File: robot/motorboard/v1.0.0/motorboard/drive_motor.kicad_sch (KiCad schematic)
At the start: 2 parts

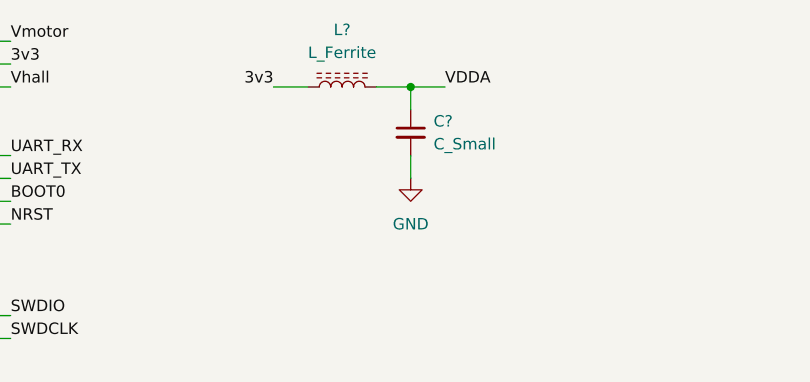
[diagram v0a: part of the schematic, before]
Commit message: finished MCU, SD, LED, DIP, and Vbatt mon. cube_hal updated
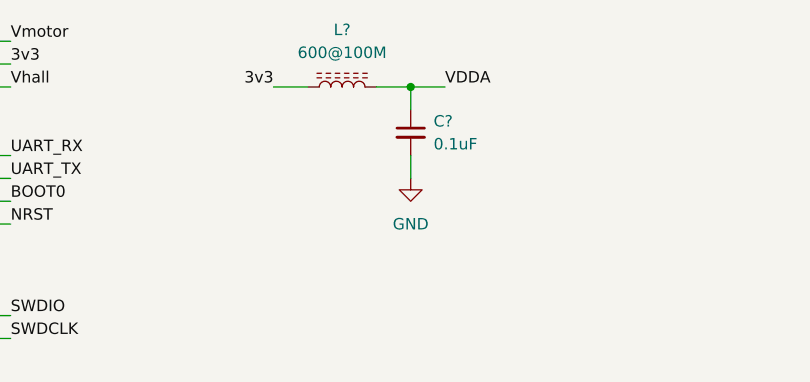
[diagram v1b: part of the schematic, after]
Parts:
- C?: value C_Small -> 0.1uF
- L?: value L_Ferrite -> 600@100M
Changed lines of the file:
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@@
     (in_bom yes) (on_board yes)
     (property "Reference" "L?" (id 0) (at 74.93 19.05 90))
-    (property "Value" "L_Ferrite" (id 1) (at 74.93 21.59 90))
+    (property "Value" "600@100M" (id 1) (at 74.93 21.59 90))
     (property "Footprint" "" (id 2) (at 74.93 25.4 0)
       (effects (font (size 1.27 1.27)) hide)
     )
-    (property "Datasheet" "~" (id 3) (at 74.93 25.4 0)
+    (property "Datasheet" "https://www.digikey.com/en/products/detail/tdk-corporation/MMZ1608B601CTAH0/600533" (id 3) (at 74.93 25.4 0)
       (effects (font (size 1.27 1.27)) hide)
     )
@@
       (effects (font (size 1.27 1.27)) (justify left))
     )
-    (property "Value" "C_Small" (id 1) (at 85.09 31.7499 0)
+    (property "Value" "0.1uF" (id 1) (at 85.09 31.7499 0)
       (effects (font (size 1.27 1.27)) (justify left))
     )

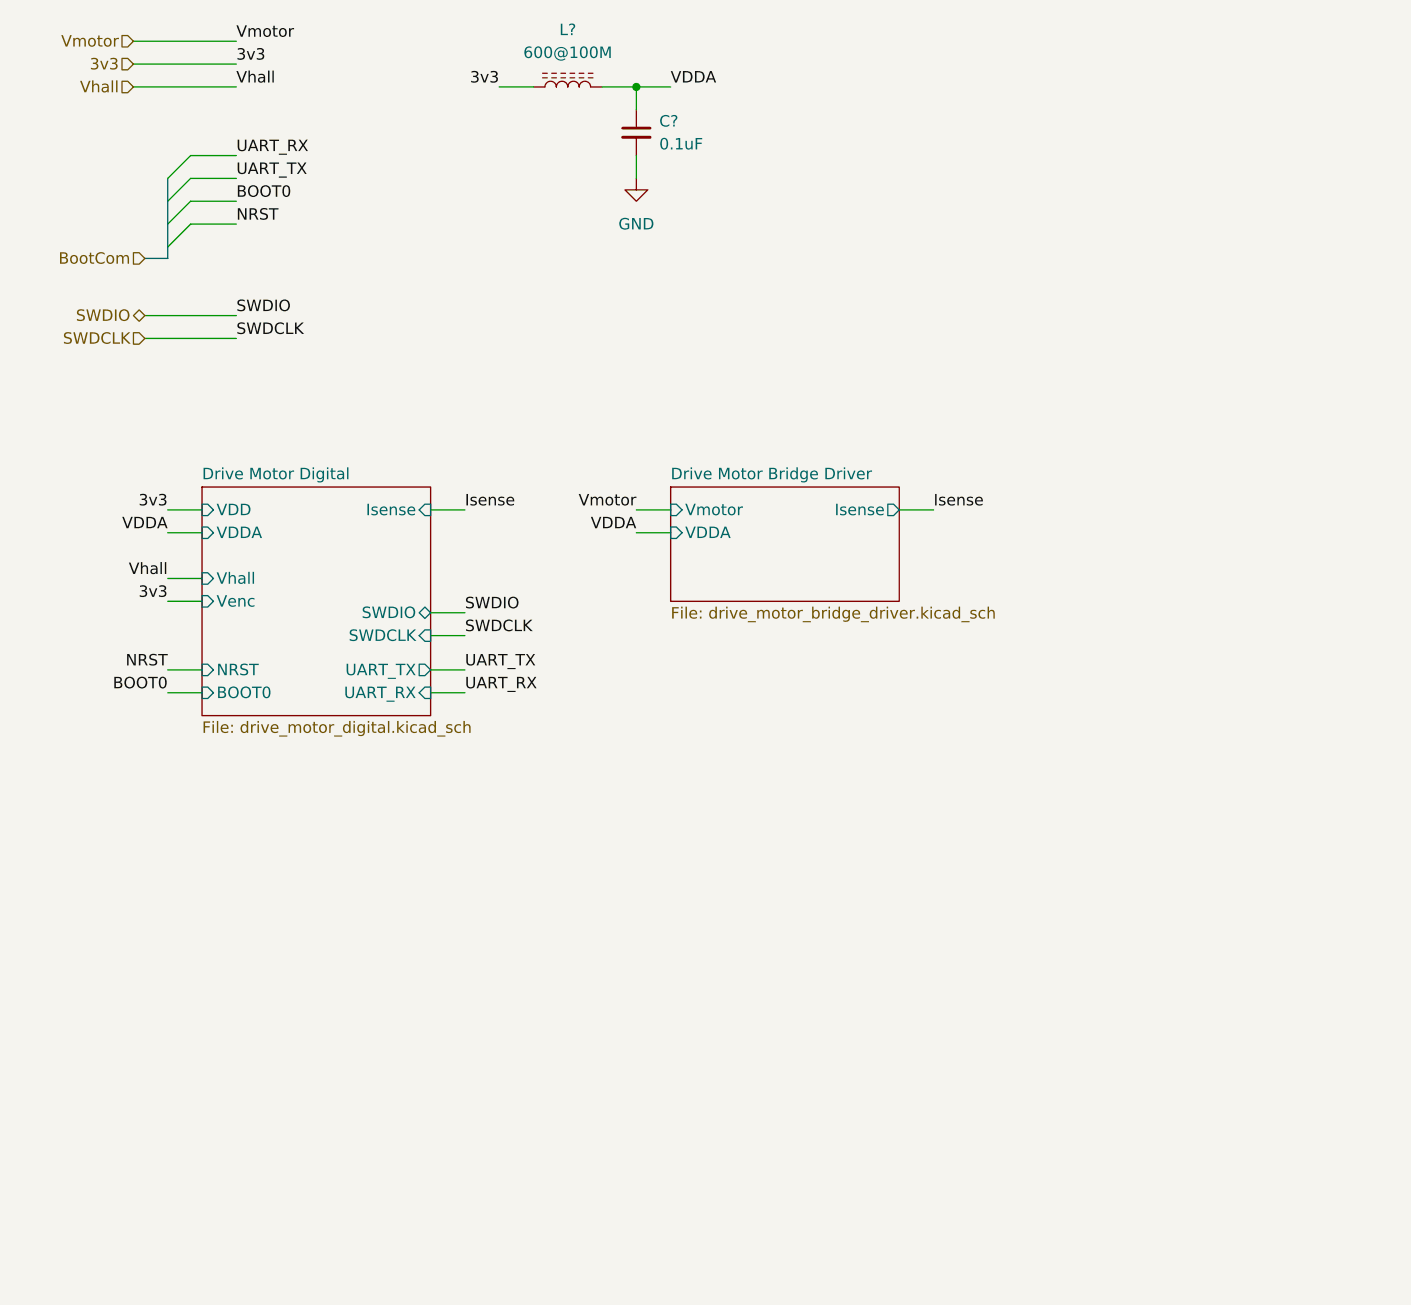
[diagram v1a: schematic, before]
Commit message: added top level bus aliases, other top level dev
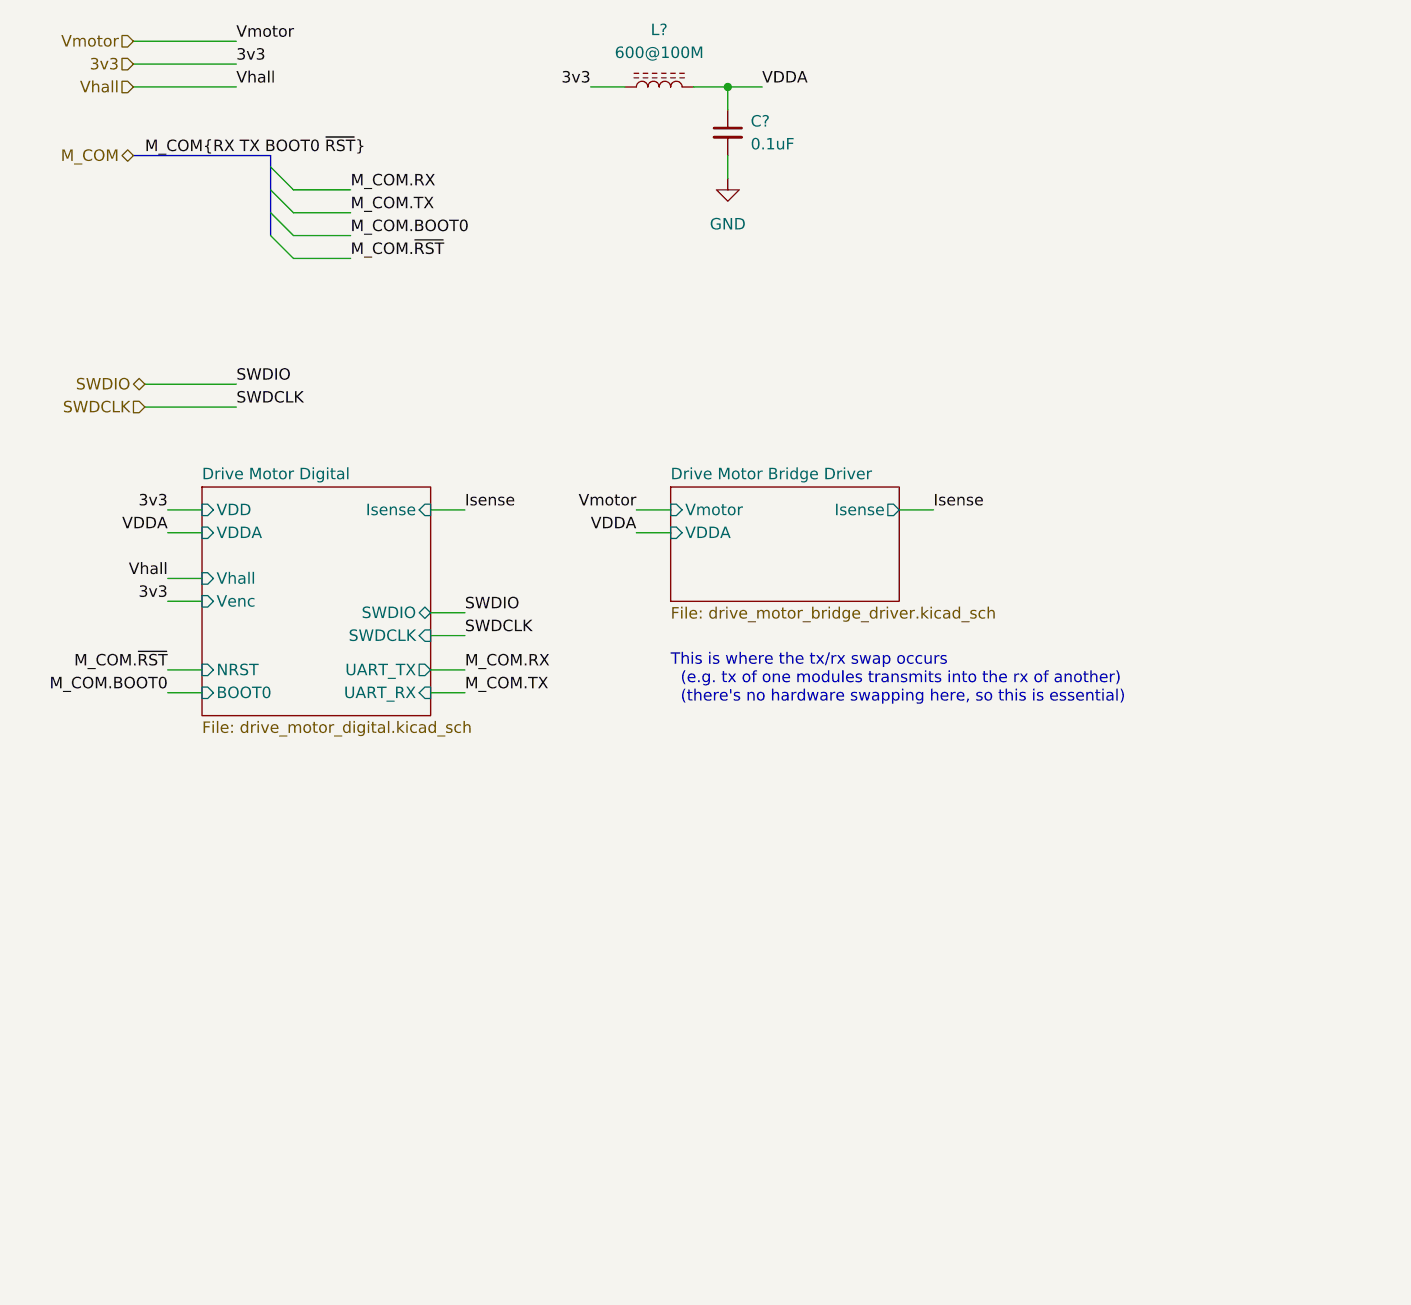
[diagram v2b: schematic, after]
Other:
- note added: "This is where the tx/rx swap occurs (e.g. tx of one modules transmits into the rx of another) (there's no hardware swapping here, so this is essential)"
- moved on the sheet: C?, L?

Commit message: bus name ERC fixes
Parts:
- gave numbers to parts that had none: 2
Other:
- sheet Drive Motor Bridge Driver ports: added {SENSE}; removed Isense
- sheet Drive Motor Digital ports: added {SENSE}; removed Isense
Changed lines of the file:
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@@
 (kicad_sch (version 20210621) (generator eeschema)
   (paper "A")
+  (bus_alias "SENSE" (members "SENSE.U" "SENSE.V"))
   (junction (at 92.71 25.4) (diameter 0.9144) (color 0 0 0 0))
   (bus_entry (at 41.91 34.29) (size 2.54 2.54)
@@
     (stroke (width 0) (type solid) (color 0 0 0 0))
   )
-  (wire (pts (xy 59.69 72.39) (xy 63.5 72.39))
-    (stroke (width 0) (type solid) (color 0 0 0 0))
-  )
   (wire (pts (xy 59.69 83.82) (xy 63.5 83.82))
     (stroke (width 0) (type solid) (color 0 0 0 0))
@@
     (stroke (width 0) (type solid) (color 0 0 0 0))
   )
-  (wire (pts (xy 111.76 72.39) (xy 115.57 72.39))
-    (stroke (width 0) (type solid) (color 0 0 0 0))
-  )
   (bus (pts (xy 26.67 33.02) (xy 41.91 33.02))
     (stroke (width 0) (type solid) (color 0 0 0 0))
   )
   (bus (pts (xy 41.91 33.02) (xy 41.91 41.91))
+    (stroke (width 0) (type solid) (color 0 0 0 0))
+  )
+  (bus (pts (xy 59.69 72.39) (xy 63.5 72.39))
+    (stroke (width 0) (type solid) (color 0 0 0 0))
+  )
+  (bus (pts (xy 111.76 72.39) (xy 115.57 72.39))
     (stroke (width 0) (type solid) (color 0 0 0 0))
   )
@@
     (effects (font (size 1.27 1.27)) (justify left bottom))
   )
-  (label "Isense" (at 63.5 72.39 0)
+  (label "{SENSE}" (at 63.5 72.39 0)
     (effects (font (size 1.27 1.27)) (justify left bottom))
   )
@@
     (effects (font (size 1.27 1.27)) (justify left bottom))
   )
-  (label "Isense" (at 115.57 72.39 0)
+  (label "{SENSE}" (at 115.57 72.39 0)
     (effects (font (size 1.27 1.27)) (justify left bottom))
   )
@@
     (effects (font (size 1.27 1.27)) (justify right))
   )
-  (hierarchical_label "M_COM" (shape bidirectional) (at 26.67 33.02 180)
+  (hierarchical_label "{M_COM}" (shape bidirectional) (at 26.67 33.02 180)
     (effects (font (size 1.27 1.27)) (justify right))
   )
@@
   (symbol (lib_id "power:GND") (at 92.71 35.56 0)
     (in_bom yes) (on_board yes) (fields_autoplaced)
-    (property "Reference" "#PWR?" (id 0) (at 92.71 41.91 0)
+    (property "Reference" "#PWR062" (id 0) (at 92.71 41.91 0)
       (effects (font (size 1.27 1.27)) hide)
     )
@@
   (symbol (lib_id "Device:L_Ferrite") (at 85.09 25.4 90)
     (in_bom yes) (on_board yes)
-    (property "Reference" "L?" (id 0) (at 85.09 19.05 90))
+    (property "Reference" "L2" (id 0) (at 85.09 19.05 90))
     (property "Value" "600@100M" (id 1) (at 85.09 21.59 90))
     (property "Footprint" "" (id 2) (at 85.09 25.4 0)
@@
   (symbol (lib_id "Device:C_Small") (at 92.71 30.48 0)
     (in_bom yes) (on_board yes) (fields_autoplaced)
-    (property "Reference" "C?" (id 0) (at 95.25 29.2099 0)
+    (property "Reference" "C14" (id 0) (at 95.25 29.2099 0)
       (effects (font (size 1.27 1.27)) (justify left))
     )
@@
       (effects (font (size 1.27 1.27)) (justify left))
     )
-    (pin "Isense" output (at 111.76 72.39 0)
+    (pin "{SENSE}" input (at 111.76 72.39 0)
       (effects (font (size 1.27 1.27)) (justify right))
     )
@@
       (effects (font (size 1.27 1.27)) (justify left))
     )
-    (pin "Isense" input (at 59.69 72.39 0)
-      (effects (font (size 1.27 1.27)) (justify right))
-    )
+    (pin "{SENSE}" input (at 59.69 72.39 0)
+      (effects (font (size 1.27 1.27)) (justify right))
+    )

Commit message: passing ERC
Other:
- moved on the sheet: L2
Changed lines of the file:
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@@
 (kicad_sch (version 20210621) (generator eeschema)
   (paper "A")
-  (bus_alias "SENSE" (members "SENSE.U" "SENSE.V"))
+  (bus_alias "SENSE" (members "SENSE.U" "SENSE.V" "SENSE.W"))
   (junction (at 92.71 25.4) (diameter 0.9144) (color 0 0 0 0))
   (bus_entry (at 41.91 34.29) (size 2.54 2.54)
@@
     (stroke (width 0) (type solid) (color 0 0 0 0))
   )
-  (wire (pts (xy 77.47 25.4) (xy 81.28 25.4))
+  (wire (pts (xy 72.39 25.4) (xy 76.2 25.4))
     (stroke (width 0) (type solid) (color 0 0 0 0))
   )
@@
     (stroke (width 0) (type solid) (color 0 0 0 0))
   )
-  (wire (pts (xy 88.9 25.4) (xy 92.71 25.4))
+  (wire (pts (xy 83.82 25.4) (xy 92.71 25.4))
     (stroke (width 0) (type solid) (color 0 0 0 0))
   )
@@
     (effects (font (size 1.27 1.27)) (justify left bottom))
   )
-  (label "3v3" (at 77.47 25.4 180)
+  (label "3v3" (at 72.39 25.4 180)
     (effects (font (size 1.27 1.27)) (justify right bottom))
   )
@@
   (symbol (lib_id "power:GND") (at 92.71 35.56 0)
     (in_bom yes) (on_board yes) (fields_autoplaced)
-    (property "Reference" "#PWR062" (id 0) (at 92.71 41.91 0)
+    (property "Reference" "#PWR0122" (id 0) (at 92.71 41.91 0)
       (effects (font (size 1.27 1.27)) hide)
     )
@@
     (pin "1")
   )
-  (symbol (lib_id "Device:L_Ferrite") (at 85.09 25.4 90)
+  (symbol (lib_id "Device:L_Ferrite") (at 80.01 25.4 90)
     (in_bom yes) (on_board yes)
-    (property "Reference" "L2" (id 0) (at 85.09 19.05 90))
-    (property "Value" "600@100M" (id 1) (at 85.09 21.59 90))
-    (property "Footprint" "" (id 2) (at 85.09 25.4 0)
-      (effects (font (size 1.27 1.27)) hide)
-    )
-    (property "Datasheet" "https://www.digikey.com/en/products/detail/tdk-corporation/MMZ1608B601CTAH0/600533" (id 3) (at 85.09 25.4 0)
-      (effects (font (size 1.27 1.27)) hide)
-    )
+    (property "Reference" "L2" (id 0) (at 80.01 19.05 90))
+    (property "Value" "600@100M" (id 1) (at 80.01 21.59 90))
+    (property "Footprint" "" (id 2) (at 80.01 25.4 0)
+      (effects (font (size 1.27 1.27)) hide)
+    )
+    (property "Datasheet" "https://www.digikey.com/en/products/detail/tdk-corporation/MMZ1608B601CTAH0/600533" (id 3) (at 80.01 25.4 0)
+      (effects (font (size 1.27 1.27)) hide)
+    )

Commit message: capacitor footprint assn
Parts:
- C14: footprint (none) -> Capacitor_SMD:C_0402_1005Metric_Pad0.74x0.62mm_HandSolder
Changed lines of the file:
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@@
   (symbol (lib_id "power:GND") (at 92.71 35.56 0)
     (in_bom yes) (on_board yes) (fields_autoplaced)
-    (property "Reference" "#PWR0122" (id 0) (at 92.71 41.91 0)
+    (property "Reference" "#PWR062" (id 0) (at 92.71 41.91 0)
       (effects (font (size 1.27 1.27)) hide)
     )
@@
       (effects (font (size 1.27 1.27)) (justify left))
     )
-    (property "Footprint" "" (id 2) (at 92.71 30.48 0)
+    (property "Footprint" "Capacitor_SMD:C_0402_1005Metric_Pad0.74x0.62mm_HandSolder" (id 2) (at 92.71 30.48 0)
       (effects (font (size 1.27 1.27)) hide)
     )
